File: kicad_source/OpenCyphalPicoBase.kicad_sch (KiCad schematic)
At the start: 49 parts, among them CN1 RASPBERRYPI_PICO, CN11 DNI, CN12 S3B-PH-SM4-TB, CN2 SM04B-SRSS-TB, CN3 SM04B-SRSS-TB, CN6 691322310002, CN7 DNI, CN8 DNI, SW1 PTS636 SM43 SMTR LFS, U3 M24C64-RMN6TP

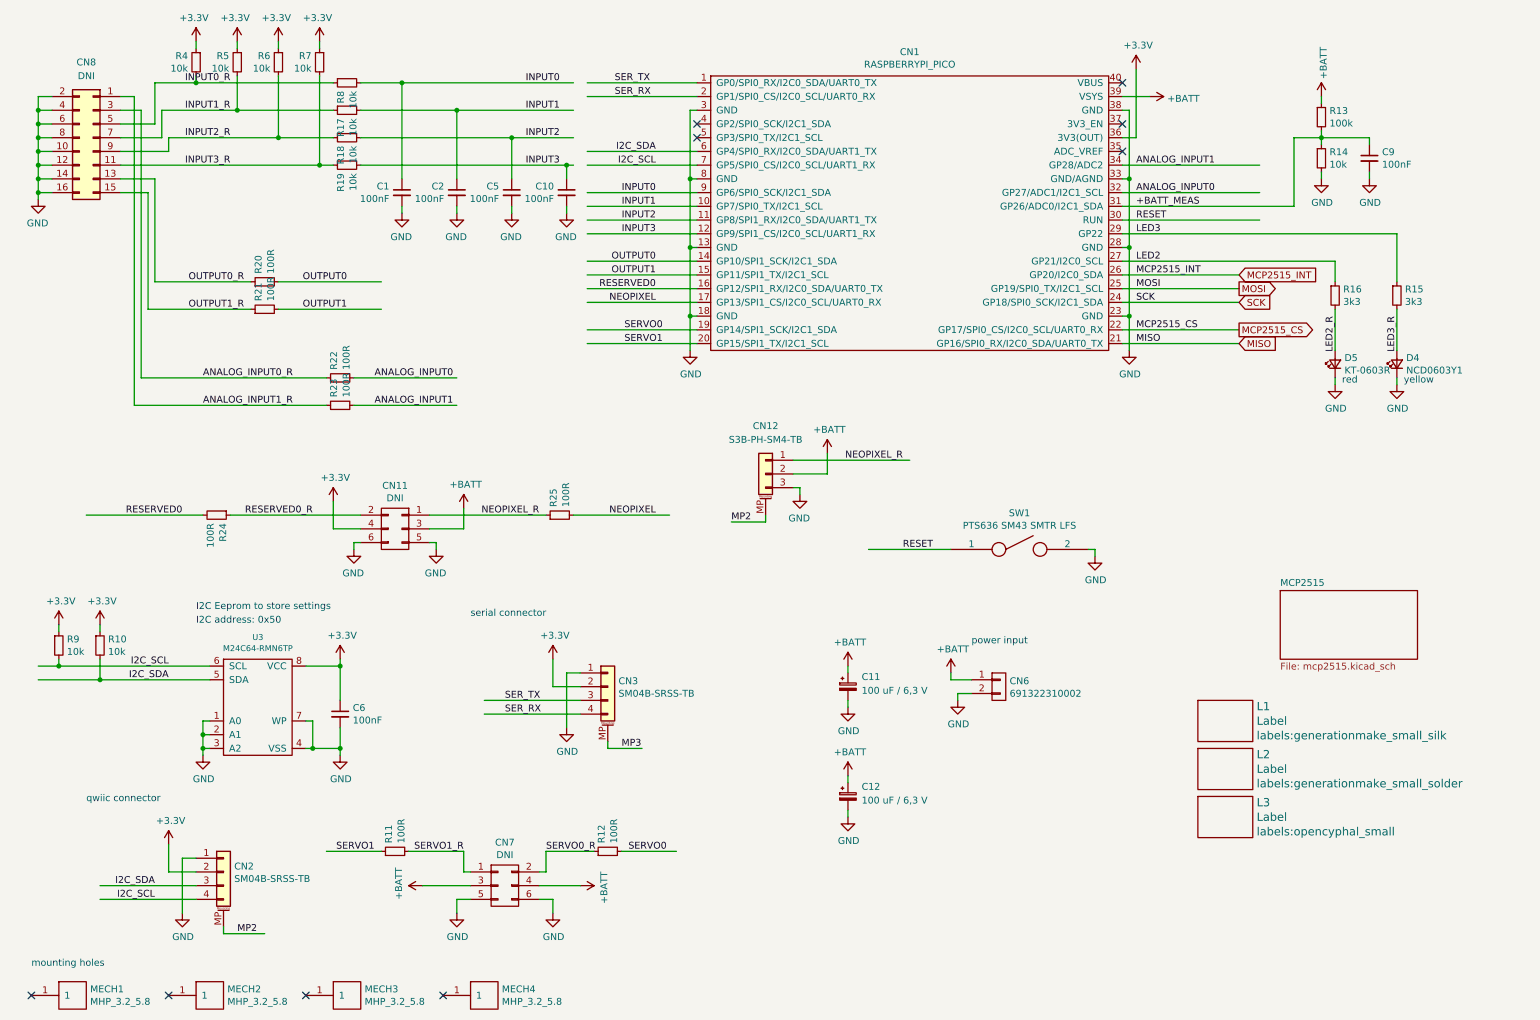
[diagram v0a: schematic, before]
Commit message: combined CN6, CN8 and CN11 into one connector
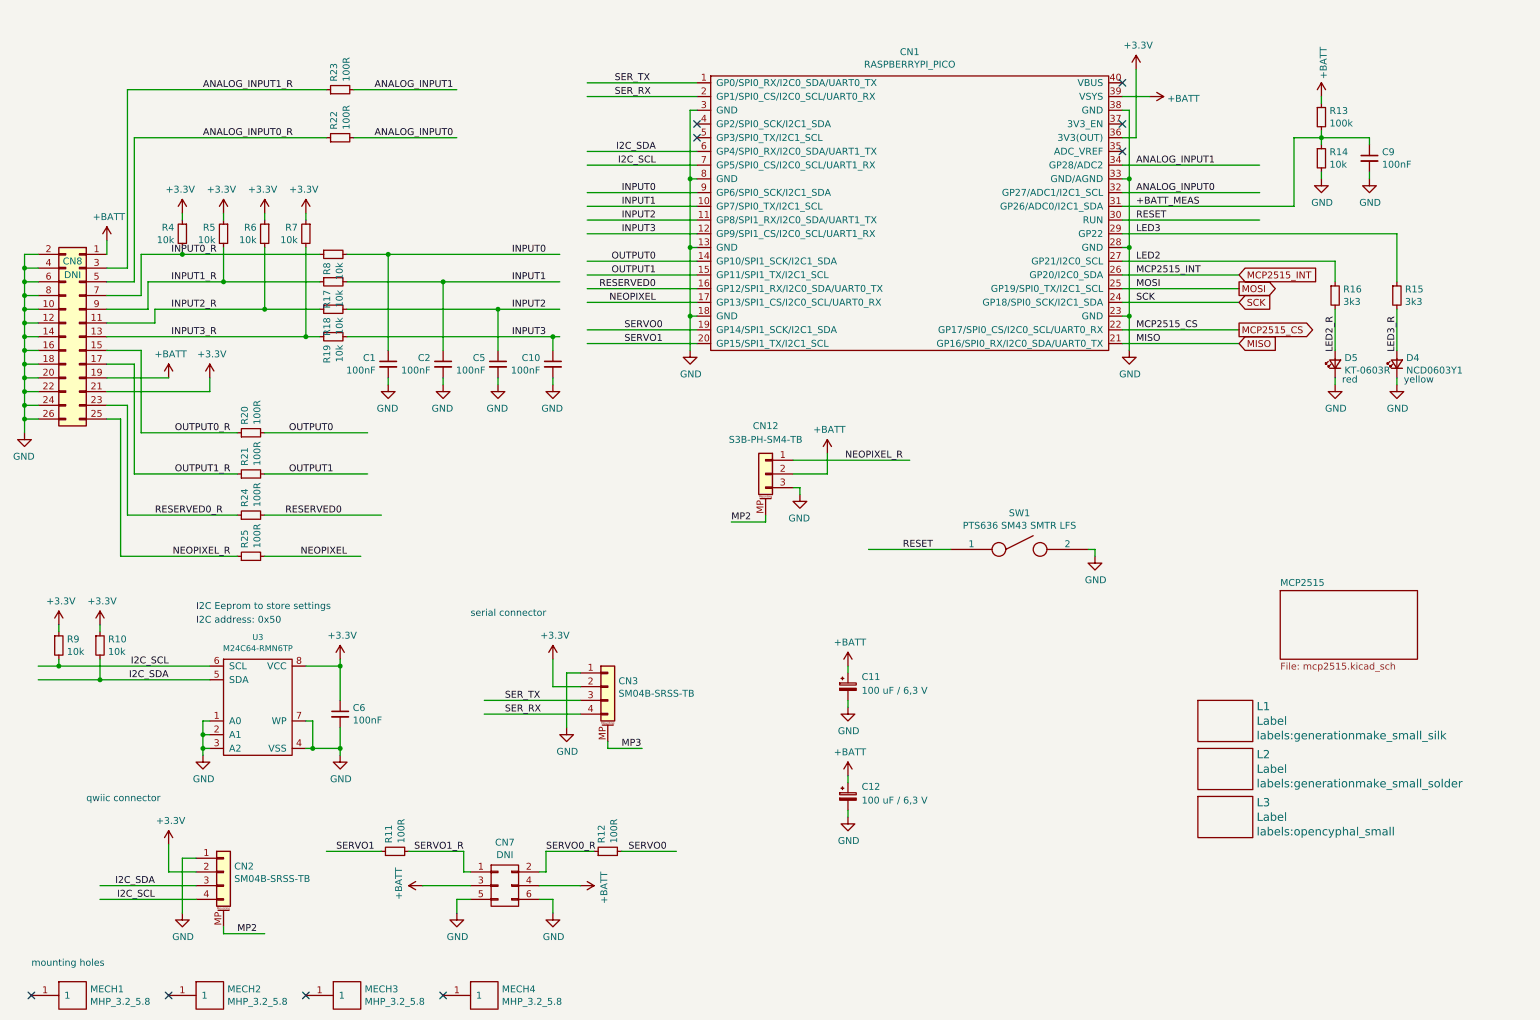
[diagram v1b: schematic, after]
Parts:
- removed CN11: DNI, Connector_PinHeader_2.54mm:PinHeader_2x03_P2.54mm_Vertical, symbol OpenCyphalPicoBase-rescue:CONN_02X03-mechanical-connectors
- removed CN6: 691322310002, CON_wuerth:WR-TBL_691322310002, symbol OpenCyphalPicoBase-rescue:CONN_01X02-mechanical-connectors
- CN8: footprint Connector_PinHeader_2.54mm:PinHeader_2x08_P2.54mm_Vertical -> Connector_PinHeader_2.54mm:PinHeader_2x13_P2.54mm_Vertical; symbol Connector_Generic:Conn_02x08_Odd_Even -> Connector_Generic:Conn_02x13_Odd_Even; now in the parts list
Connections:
- net +3V3: now also CN8.21 (Pin_21)
- net +BATT: now also CN8.1 (Pin_1), CN8.19 (Pin_19)
- net ANALOG_INPUT0_R: now also CN8.5 (Pin_5); no longer CN8.3 (Pin_3)
- net ANALOG_INPUT1_R: now also CN8.3 (Pin_3); no longer CN8.1 (Pin_1)
- net GND: now also CN8.18 (Pin_18), CN8.20 (Pin_20), CN8.22 (Pin_22), CN8.24 (Pin_24), CN8.26 (Pin_26)
- net INPUT0_R: now also CN8.7 (Pin_7); no longer CN8.5 (Pin_5)
- net INPUT1_R: now also CN8.9 (Pin_9); no longer CN8.7 (Pin_7)
- net INPUT2_R: now also CN8.11 (Pin_11); no longer CN8.9 (Pin_9)
- net INPUT3_R: now also CN8.13 (Pin_13); no longer CN8.11 (Pin_11)
- net NEOPIXEL_R: now also CN8.25 (Pin_25)
- net OUTPUT0_R: now also CN8.15 (Pin_15); no longer CN8.13 (Pin_13)
- net OUTPUT1_R: now also CN8.17 (Pin_17); no longer CN8.15 (Pin_15)
- net RESERVED0_R: now also CN8.23 (Pin_23)
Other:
- note removed: "power input"
- moved on the sheet: C1, C10, C2, C5, R17, R18, R19, R20, R21, R22, R23, R24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

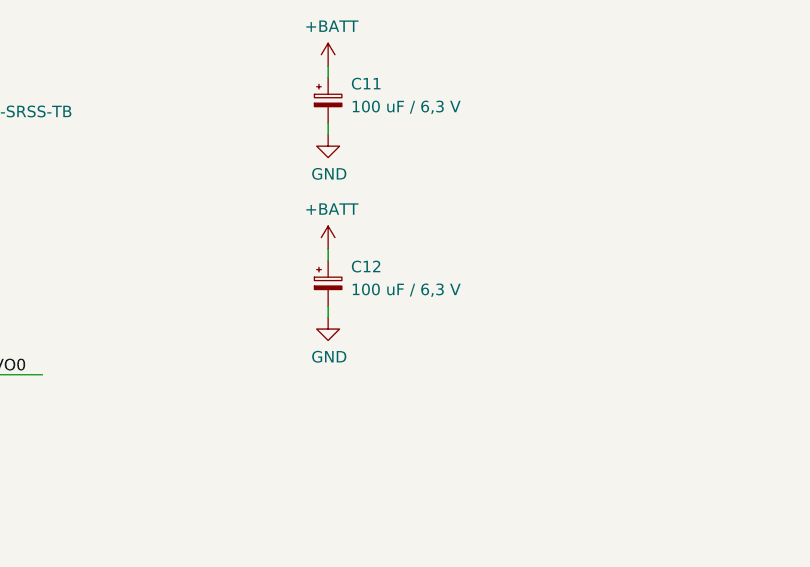
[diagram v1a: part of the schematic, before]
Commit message: removed C12, added CAN protection, updated schematic
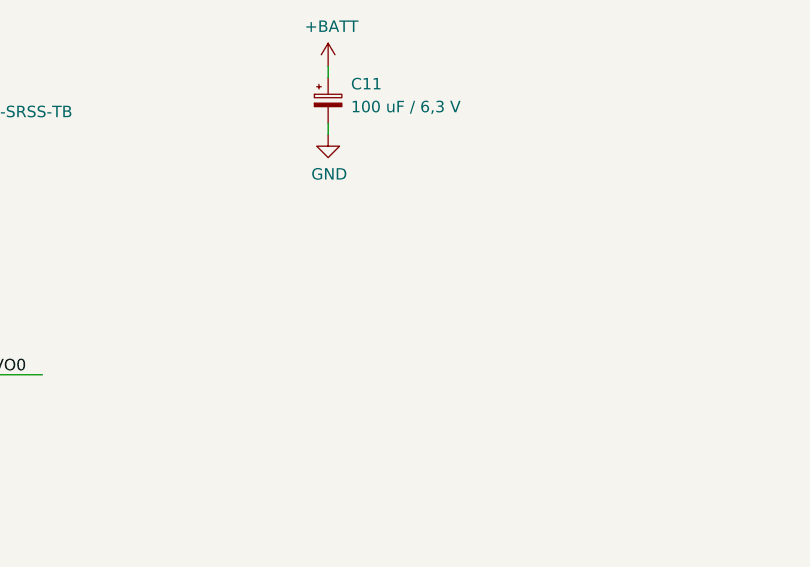
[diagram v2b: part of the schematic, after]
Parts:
- removed C12: 100 uF / 6,3 V, Capacitor_SMD:CP_Elec_5x5.3, symbol Device:C_Polarized_Small
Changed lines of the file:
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@@
-    (stroke (width 0) (type default) (color 0 0 0 0))
-  )
-  (wire (pts (xy 168.91 152.4) (xy 168.91 153.67))
     (stroke (width 0) (type default) (color 0 0 0 0))
   )
@@
   )
   (wire (pts (xy 83.82 73.66) (xy 83.82 55.88))
-    (stroke (width 0) (type default) (color 0 0 0 0))
-  )
-  (wire (pts (xy 168.91 158.75) (xy 168.91 160.02))
     (stroke (width 0) (type default) (color 0 0 0 0))
   )
@@
     (pin "1")
   )
-  (symbol (lib_id "Device:C_Polarized_Small") (at 168.91 156.21 0) (unit 1)
-    (in_bom yes) (on_board yes) (fields_autoplaced)
-    (property "Reference" "C12" (id 0) (at 171.45 154.3938 0)
-      (effects (font (size 1.27 1.27)) (justify left))
-    )
-    (property "Value" "100 uF / 6,3 V" (id 1) (at 171.45 156.9338 0)
-      (effects (font (size 1.27 1.27)) (justify left))
-    )
-    (property "Footprint" "Capacitor_SMD:CP_Elec_5x5.3" (id 2) (at 168.91 156.21 0)
-      (effects (font (size 1.27 1.27)) hide)
-    )
-    (property "Datasheet" "~" (id 3) (at 168.91 156.21 0)
-      (effects (font (size 1.27 1.27)) hide)
-    )
-    (property "LCSC" "C3001204" (id 4) (at 168.91 156.21 0)
-      (effects (font (size 1.27 1.27)) hide)
-    )
-    (pin "1")
-    (pin "2")
-  )
   (symbol (lib_id "OpenCyphalPicoBase-rescue:GND-power-supply") (at 168.91 139.7 0) (unit 1)
     (in_bom yes) (on_board yes)
@@
     (property "Footprint" "" (id 2) (at 168.91 139.7 0))
     (property "Datasheet" "" (id 3) (at 168.91 139.7 0))
-    (pin "1")
-  )
-  (symbol (lib_id "OpenCyphalPicoBase-rescue:+BATT-power-supply") (at 168.91 152.4 0) (unit 1)
-    (in_bom yes) (on_board yes)
-    (property "Reference" "#PWR052" (id 0) (at 168.91 156.21 0)
-      (effects (font (size 1.27 1.27)) hide)
-    )
-    (property "Value" "+BATT" (id 1) (at 169.291 148.0058 0))
-    (property "Footprint" "" (id 2) (at 168.91 152.4 0))
-    (property "Datasheet" "" (id 3) (at 168.91 152.4 0))
     (pin "1")
   )
@@
     (pin "1")
   )
-  (symbol (lib_id "OpenCyphalPicoBase-rescue:GND-power-supply") (at 168.91 160.02 0) (unit 1)
-    (in_bom yes) (on_board yes)
-    (property "Reference" "#PWR053" (id 0) (at 168.91 166.37 0)
-      (effects (font (size 1.27 1.27)) hide)
-    )
-    (property "Value" "GND" (id 1) (at 169.037 164.4142 0))
-    (property "Footprint" "" (id 2) (at 168.91 160.02 0))
-    (property "Datasheet" "" (id 3) (at 168.91 160.02 0))
-    (pin "1")
-  )
   (symbol (lib_id "OpenCyphalPicoBase-rescue:+BATT-power-supply") (at 31.75 53.34 0) (unit 1)
     (in_bom yes) (on_board yes)
@@
       (reference "#PWR019") (unit 1) (value "+3.3V") (footprint "")
     )
+    (path "/00000000-0000-0000-0000-00005ed92f9c/1916be01-9561-4e8d-aead-26330711ff23"
+      (reference "#PWR020") (unit 1) (value "GND") (footprint "")
+    )
     (path "/00000000-0000-0000-0000-00005ed92f9c/00000000-0000-0000-0000-00005eda8fcf"
       (reference "#PWR022") (unit 1) (value "+3.3V") (footprint "")
@@
       (reference "#PWR047") (unit 1) (value "GND") (footprint "")
     )
-    (path "/1b9ed98e-9794-43b6-9513-6b70efa279c6"
-      (reference "#PWR052") (unit 1) (value "+BATT") (footprint "")
-    )
-    (path "/c3979e04-2e0c-4de7-a444-c8166b6cadd1"
-      (reference "#PWR053") (unit 1) (value "GND") (footprint "")
-    )
     (path "/00000000-0000-0000-0000-000062c052ff"
       (reference "#PWR054") (unit 1) (value "GND") (footprint "")
@@
       (reference "C11") (unit 1) (value "100 uF / 6,3 V") (footprint "Capacitor_SMD:CP_Elec_5x5.3")
     )
-    (path "/0c3f626b-e5ab-4546-95f5-05afc50b086b"
-      (reference "C12") (unit 1) (value "100 uF / 6,3 V") (footprint "Capacitor_SMD:CP_Elec_5x5.3")
-    )
     (path "/00000000-0000-0000-0000-0000629e332f"
       (reference "CN1") (unit 1) (value "RASPBERRYPI_PICO") (footprint "generationmake:RASPI_PICO_SOLDER_Kopie")
@@
       (reference "CN12") (unit 1) (value "S3B-PH-SM4-TB") (footprint "Connector_JST:JST_PH_S3B-PH-SM4-TB_1x03-1MP_P2.00mm_Horizontal")
     )
+    (path "/00000000-0000-0000-0000-00005ed92f9c/1c7e72c3-a858-4ad7-b8a5-648cc04b24c6"
+      (reference "D1") (unit 1) (value "NUP2105L") (footprint "Package_TO_SOT_SMD:SOT-23")
+    )
     (path "/00000000-0000-0000-0000-00005ed92f9c/00000000-0000-0000-0000-000062500ccf"

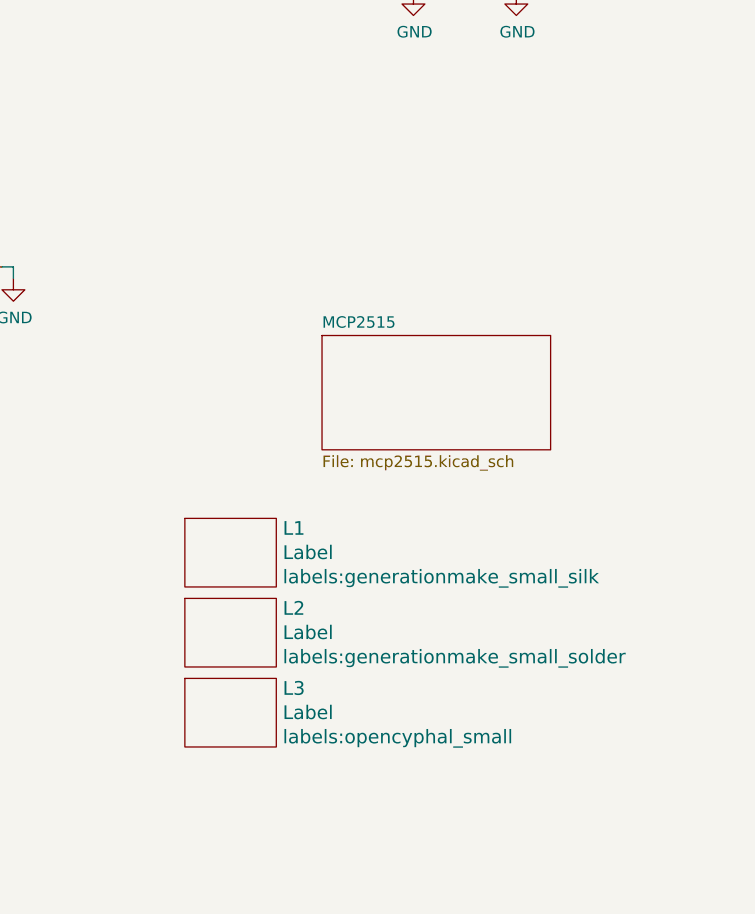
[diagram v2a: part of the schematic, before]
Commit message: added qwiic logo, made DRC
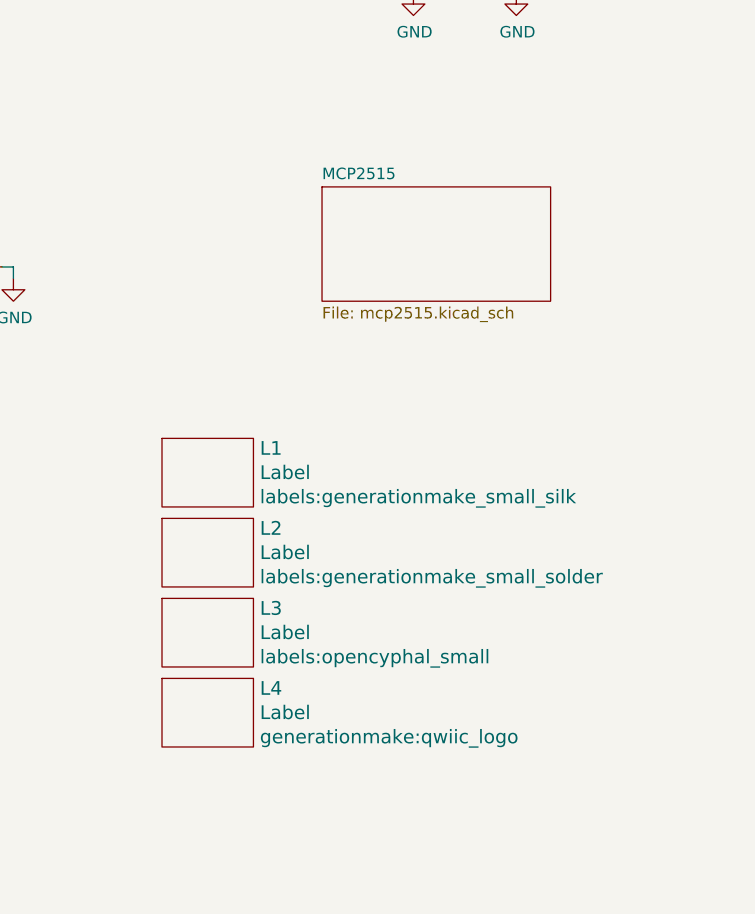
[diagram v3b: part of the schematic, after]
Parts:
- added L4: Label, generationmake:qwiic_logo, symbol OpenCyphalPicoBase-rescue:Label-devices
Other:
- moved on the sheet: L1, L2, L3
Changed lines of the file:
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@@
   (title_block
     (title "OpenCyphalPicoBase")
-    (date "2023-08-08")
+    (date "2023-08-09")
     (rev "0.3")
     (company "generationmake")
@@
     (pin "1")
   )
-  (symbol (lib_id "OpenCyphalPicoBase-rescue:Label-devices") (at 238.76 142.24 0) (unit 1)
+  (symbol (lib_id "OpenCyphalPicoBase-rescue:Label-devices") (at 236.22 133.35 0) (unit 1)
     (in_bom no) (on_board yes)
-    (property "Reference" "L1" (id 0) (at 244.5512 139.5476 0)
+    (property "Reference" "L1" (id 0) (at 242.0112 130.6576 0)
       (effects (font (size 1.524 1.524)) (justify left))
     )
-    (property "Value" "Label" (id 1) (at 244.5512 142.24 0)
+    (property "Value" "Label" (id 1) (at 242.0112 133.35 0)
       (effects (font (size 1.524 1.524)) (justify left))
     )
-    (property "Footprint" "labels:generationmake_small_silk" (id 2) (at 244.5512 144.9324 0)
+    (property "Footprint" "labels:generationmake_small_silk" (id 2) (at 242.0112 136.0424 0)
       (effects (font (size 1.524 1.524)) (justify left))
     )
-    (property "Datasheet" "" (id 3) (at 238.76 142.24 0)
+    (property "Datasheet" "" (id 3) (at 236.22 133.35 0)
       (effects (font (size 1.524 1.524)))
     )
   )
-  (symbol (lib_id "OpenCyphalPicoBase-rescue:Label-devices") (at 238.76 151.13 0) (unit 1)
+  (symbol (lib_id "OpenCyphalPicoBase-rescue:Label-devices") (at 236.22 142.24 0) (unit 1)
     (in_bom no) (on_board yes)
-    (property "Reference" "L2" (id 0) (at 244.5512 148.4376 0)
+    (property "Reference" "L2" (id 0) (at 242.0112 139.5476 0)
       (effects (font (size 1.524 1.524)) (justify left))
     )
-    (property "Value" "Label" (id 1) (at 244.5512 151.13 0)
+    (property "Value" "Label" (id 1) (at 242.0112 142.24 0)
       (effects (font (size 1.524 1.524)) (justify left))
     )
-    (property "Footprint" "labels:generationmake_small_solder" (id 2) (at 244.5512 153.8224 0)
+    (property "Footprint" "labels:generationmake_small_solder" (id 2) (at 242.0112 144.9324 0)
       (effects (font (size 1.524 1.524)) (justify left))
     )
-    (property "Datasheet" "" (id 3) (at 238.76 151.13 0)
+    (property "Datasheet" "" (id 3) (at 236.22 142.24 0)
       (effects (font (size 1.524 1.524)))
     )
   )
-  (symbol (lib_id "OpenCyphalPicoBase-rescue:Label-devices") (at 238.76 160.02 0) (unit 1)
+  (symbol (lib_id "OpenCyphalPicoBase-rescue:Label-devices") (at 236.22 151.13 0) (unit 1)
     (in_bom no) (on_board yes)
-    (property "Reference" "L3" (id 0) (at 244.5512 157.3276 0)
+    (property "Reference" "L3" (id 0) (at 242.0112 148.4376 0)
       (effects (font (size 1.524 1.524)) (justify left))
     )
-    (property "Value" "Label" (id 1) (at 244.5512 160.02 0)
+    (property "Value" "Label" (id 1) (at 242.0112 151.13 0)
       (effects (font (size 1.524 1.524)) (justify left))
     )
-    (property "Footprint" "labels:opencyphal_small" (id 2) (at 244.5512 162.7124 0)
+    (property "Footprint" "labels:opencyphal_small" (id 2) (at 242.0112 153.8224 0)
       (effects (font (size 1.524 1.524)) (justify left))
     )
-    (property "Datasheet" "" (id 3) (at 238.76 160.02 0)
+    (property "Datasheet" "" (id 3) (at 236.22 151.13 0)
       (effects (font (size 1.524 1.524)))
     )
@@
     (pin "1")
   )
+  (symbol (lib_id "OpenCyphalPicoBase-rescue:Label-devices") (at 236.22 160.02 0) (unit 1)
+    (in_bom no) (on_board yes)
+    (property "Reference" "L4" (id 0) (at 242.0112 157.3276 0)
+      (effects (font (size 1.524 1.524)) (justify left))
+    )
+    (property "Value" "Label" (id 1) (at 242.0112 160.02 0)
+      (effects (font (size 1.524 1.524)) (justify left))
+    )
+    (property "Footprint" "generationmake:qwiic_logo" (id 2) (at 242.0112 162.7124 0)
+      (effects (font (size 1.524 1.524)) (justify left))
+    )
+    (property "Datasheet" "" (id 3) (at 236.22 160.02 0)
+      (effects (font (size 1.524 1.524)))
+    )
+  )
   (symbol (lib_id "OpenCyphalPicoBase-rescue:+BATT-power-supply") (at 31.75 53.34 0) (unit 1)
     (in_bom yes) (on_board yes)
@@
     (pin "1")
   )
-  (sheet (at 248.92 118.11) (size 25.4 12.7) (fields_autoplaced)
+  (sheet (at 248.92 101.6) (size 25.4 12.7) (fields_autoplaced)
     (stroke (width 0) (type solid) (color 0 0 0 0))
     (fill (color 0 0 0 0.0000))
-    (property "Sheet name" "MCP2515" (id 0) (at 248.92 117.3984 0)
+    (property "Sheet name" "MCP2515" (id 0) (at 248.92 100.8884 0)
       (effects (font (size 1.27 1.27)) (justify left bottom))
     )
-    (property "Sheet file" "mcp2515.kicad_sch" (id 1) (at 248.92 131.3946 0)
+    (property "Sheet file" "mcp2515.kicad_sch" (id 1) (at 248.92 114.8846 0)
       (effects (font (size 1.27 1.27)) (justify left top))
     )
@@
     )
     (path "/00000000-0000-0000-0000-00005ed92f9c/1c7e72c3-a858-4ad7-b8a5-648cc04b24c6"
-      (reference "D1") (unit 1) (value "NUP2105L") (footprint "Package_TO_SOT_SMD:SOT-23")
+      (reference "D1") (unit 1) (value "DNI") (footprint "Package_TO_SOT_SMD:SOT-23")
     )
     (path "/00000000-0000-0000-0000-00005ed92f9c/00000000-0000-0000-0000-000062500ccf"
@@
       (reference "L3") (unit 1) (value "Label") (footprint "labels:opencyphal_small")
     )
+    (path "/b3b51ab2-eedf-4a64-bef7-8767d2ae28a9"
+      (reference "L4") (unit 1) (value "Label") (footprint "generationmake:qwiic_logo")
+    )
     (path "/00000000-0000-0000-0000-00005e401602"
